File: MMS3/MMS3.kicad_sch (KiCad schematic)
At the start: 5 parts

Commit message: changed most of stuff to ch32L103
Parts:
- added Q1: MMBT5401 200-300, PCM_JLCPCB:Q_SOT-23, symbol PCM_JLCPCB-Transistors:PNP,MMBT5401 200-300
- added R10: 1.5kΩ, PCM_JLCPCB:R_0603, symbol PCM_JLCPCB-Resistors:0603,1.5kΩ
- added R12, R13: 5.1kΩ, PCM_JLCPCB:R_0603, symbol PCM_JLCPCB-Resistors:0603,5.1kΩ
- added TP5, TP6: TestPoint, TestPoint:TestPoint_Pad_D1.0mm, symbol Connector:TestPoint
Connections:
- net USB switch1/SEL is gone; now on net BRD_VIN: D5.2
- net GND: now also Q1.2 (E), R12.2, R13.2
- new net: Q1.1 (B), R10.2
- new net CAN.RX: TP6.1
- new net CAN.TX: TP5.1
- new net CC1: R13.1
- new net CC2: R12.1
- new net CH32L103/PC13 (TAMPER, RTC): R10.1
- new net RXD2_LED: Q1.3 (C)
- no-connect marks 2 -> 23
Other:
- removed sheet CAN_TR1
- removed sheet MCU
- removed sheet STlink-BMprobe
- removed sheet Slide-SW
- removed sheet USB HUB
- removed sheet USB switch
- removed sheet USB switch1
- removed sheet VRM
- added sheet CH32L103 (CH32L103C8T6.kicad_sch)
- sheet USBC_CONN ports: added CC1, CC2; removed none
- note added: "LDO 5V 3V3"
- note added: "USER BUTTON"
- note removed: "USB- Stealy Wheely"
- moved on the sheet: D5, H1, H2, H3, H4

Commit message: backup commit
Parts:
- removed R12, R13: 5.1kΩ, PCM_JLCPCB:R_0603, symbol PCM_JLCPCB-Resistors:0603,5.1kΩ
- removed TP5, TP6: TestPoint, TestPoint:TestPoint_Pad_D1.0mm, symbol Connector:TestPoint
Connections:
- net BRD_VIN: no longer D5.2
- net CH32L103/PC13 (TAMPER, RTC) renamed CH32L103_Wrapper/PC13
- new net USB_Data/VBUS: D5.2
- no-connect marks 23 -> 2
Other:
- sheet USBC_CONN renamed USB_Data
- removed sheet CH32L103
- added sheet CH32L103_Wrapper (CH32L103_MMS3.kicad_sch)
- added sheet Power Supply (LDO.kicad_sch)
- added sheet USB_PD (USP_PD.kicad_sch)
- sheet USB_Data ports: added none; removed CC1, CC2
- note added: "CAN"
- note added: "CHINESE"
- note added: "EEPROM"
- note added: "MCU"
- note added: "No MMS_Link USB Programmer due to budget cuts )):"
- note added: "PSU"

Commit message: kinda finished schematic
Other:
- removed sheet Power Supply
- added sheet VRM (VRM.kicad_sch)
- note removed: "CHINESE"
- note removed: "MCU"
- note removed: "PSU"

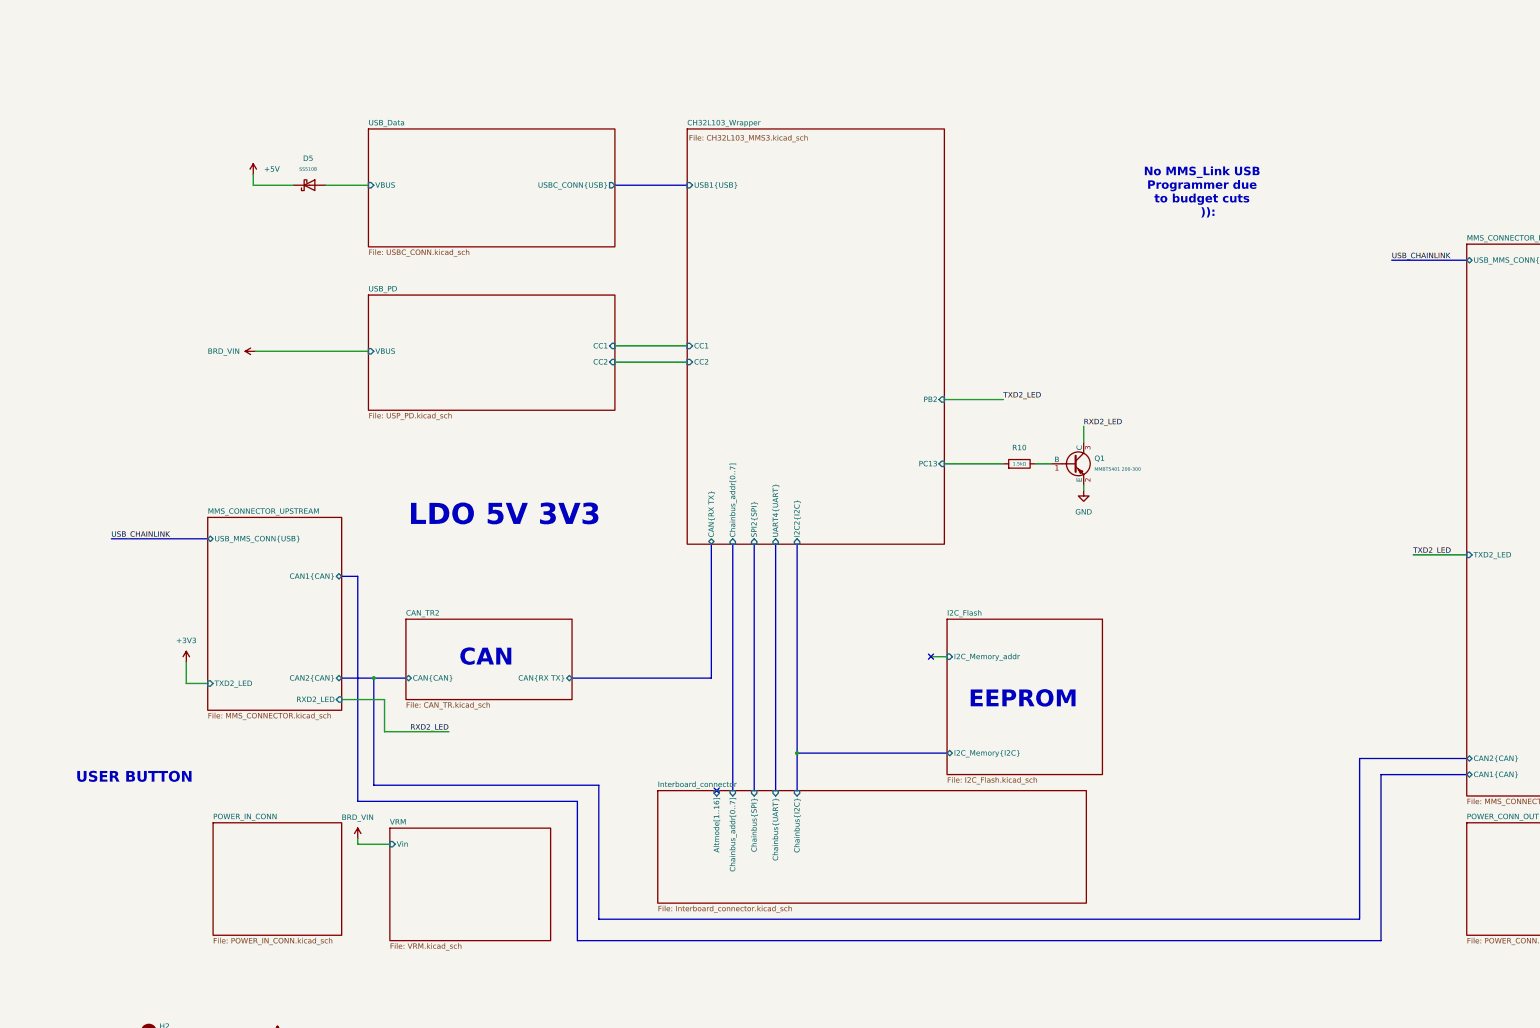
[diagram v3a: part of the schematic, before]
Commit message: updated schematic, removed annotation
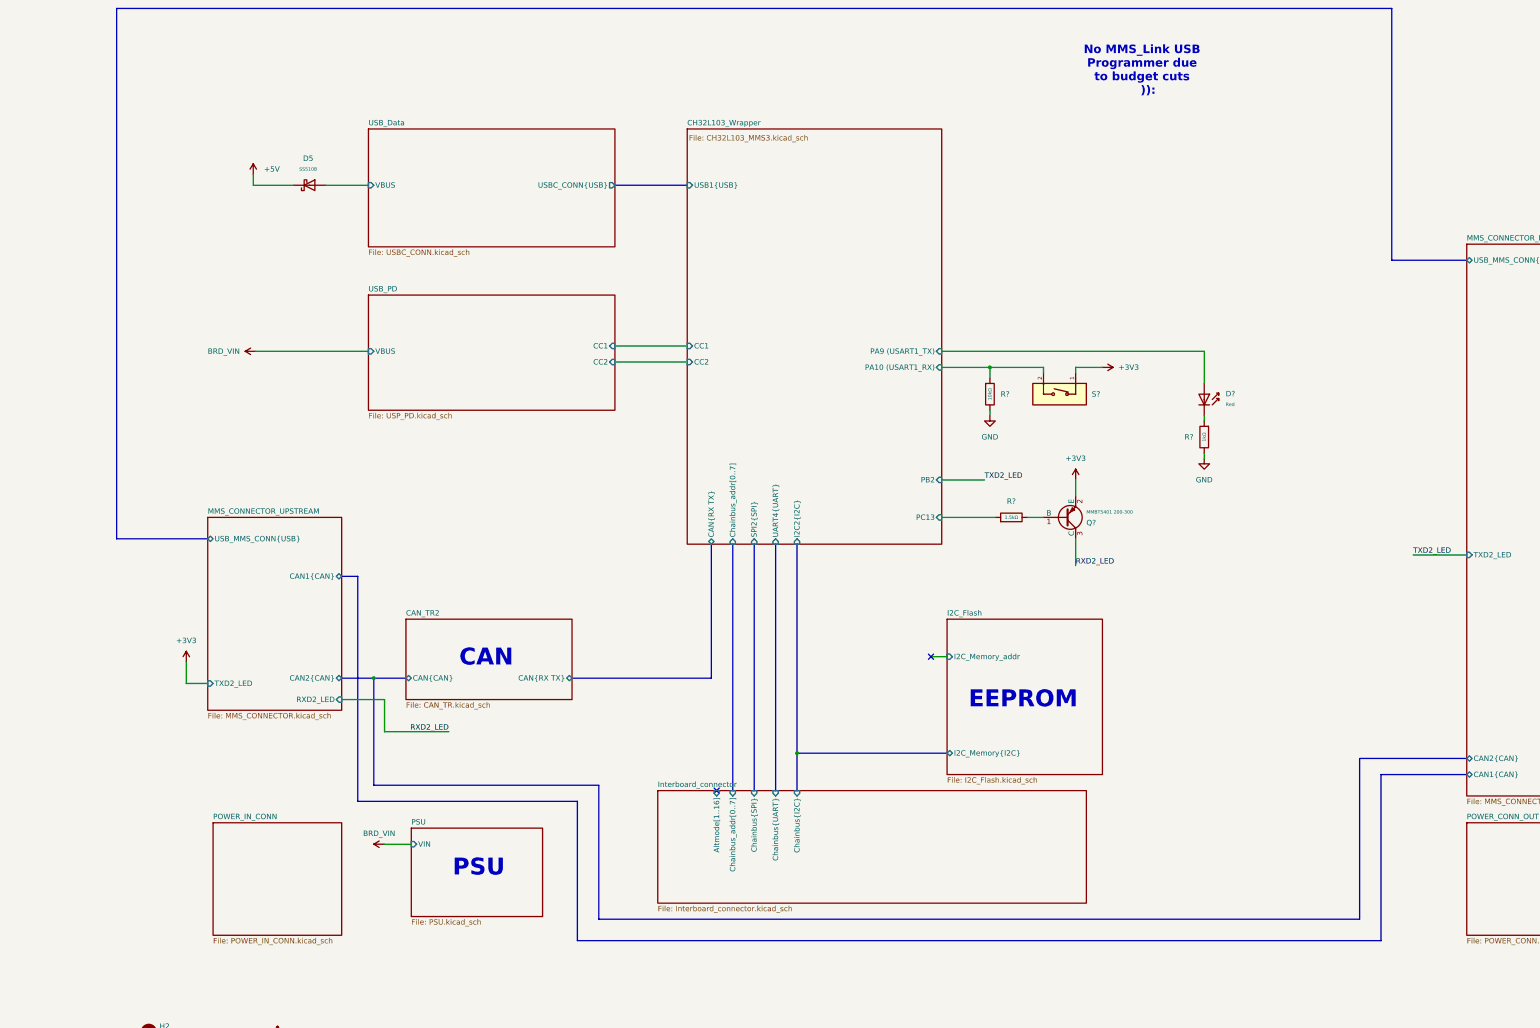
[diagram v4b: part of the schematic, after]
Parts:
- added D?: Red, PCM_JLCPCB:D_0603, symbol PCM_JLCPCB-Diodes:LED,0603,Red
- added R?: 10kΩ, PCM_JLCPCB:R_0402, symbol PCM_JLCPCB-Resistors:0402,10kΩ
- added R?: 1kΩ, PCM_JLCPCB:R_0603, symbol PCM_JLCPCB-Resistors:0603,1kΩ
- added S?: Tactile Button, 160gf, PCM_JLCPCB:SW_TS-1088-AR02016, symbol PCM_JLCPCB-Connectors_Buttons:Tactile Button, 160gf, 12V, 50mA, 4.0mm
- renumbered Q1 to Q?, R10 to R?
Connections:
- net +3V3: now also Q?.2 (E), S?.1 (A)
- net GND: now also R?.2, R?.2; no longer Q?.2 (E)
- new net: D?.1, R?.1
- new net CH32L103_Wrapper/PA10 (USART1_RX): R?.1, S?.2 (B)
- new net CH32L103_Wrapper/PA9 (USART1_TX): D?.2
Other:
- removed sheet VRM
- added sheet PSU (PSU.kicad_sch)
- sheet CH32L103_Wrapper ports: added PA10 (USART1_RX), PA9 (USART1_TX); removed none
- note added: "PSU"
- note removed: "LDO 5V 3V3"
- note removed: "USER BUTTON"
- title: MMS3 -> MMS3 CH32L103 Version
- moved on the sheet: Q?, R?

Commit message: initial PCB update
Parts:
- gave numbers to parts that had none: 6
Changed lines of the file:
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@@
 		(dnp no)
 		(fields_autoplaced yes)
-		(property "Reference" "R?"
+		(property "Reference" "R7"
 			(at 251.46 114.2999 0)
 			(show_name no)
@@
 			(project "MMS3"
 				(path "/712cea22-140d-4c92-923f-f4998caf3ecd"
-					(reference "R?")
+					(reference "R7")
 					(unit 1)
 				)
@@
 		(dnp no)
 		(fields_autoplaced yes)
-		(property "Reference" "#PWR?"
+		(property "Reference" "#PWR010"
 			(at 248.92 125.73 0)
 			(hide yes)
@@
 			(project "MMS3"
 				(path "/712cea22-140d-4c92-923f-f4998caf3ecd"
-					(reference "#PWR?")
+					(reference "#PWR010")
 					(unit 1)
 				)
@@
 		(in_pos_files yes)
 		(dnp no)
-		(property "Reference" "Q?"
+		(property "Reference" "Q1"
 			(at 271.78 144.7801 0)
 			(show_name no)
@@
 			(project "MMS3"
 				(path "/712cea22-140d-4c92-923f-f4998caf3ecd"
-					(reference "Q?")
+					(reference "Q1")
 					(unit 1)
 				)
@@
 		(dnp no)
 		(fields_autoplaced yes)
-		(property "Reference" "#PWR?"
+		(property "Reference" "#PWR012"
 			(at 271.78 107.95 0)
 			(hide yes)
@@
 			(project "MMS3"
 				(path "/712cea22-140d-4c92-923f-f4998caf3ecd"
-					(reference "#PWR?")
+					(reference "#PWR012")
 					(unit 1)
 				)
@@
 		(dnp no)
 		(fields_autoplaced yes)
-		(property "Reference" "S?"
+		(property "Reference" "S1"
 			(at 273.05 114.2999 90)
 			(show_name no)
@@
 			(project "MMS3"
 				(path "/712cea22-140d-4c92-923f-f4998caf3ecd"
-					(reference "S?")
+					(reference "S1")
 					(unit 1)
 				)
@@
 		(dnp no)
 		(fields_autoplaced yes)
-		(property "Reference" "R?"
+		(property "Reference" "R9"
 			(at 297.18 124.4599 0)
 			(show_name no)
@@
 			(project "MMS3"
 				(path "/712cea22-140d-4c92-923f-f4998caf3ecd"
-					(reference "R?")
+					(reference "R9")
 					(unit 1)
 				)
@@
 		(dnp no)
 		(fields_autoplaced yes)
-		(property "Reference" "R?"
+		(property "Reference" "R8"
 			(at 254 139.7 90)
 			(show_name no)
@@
 			(project "MMS3"
 				(path "/712cea22-140d-4c92-923f-f4998caf3ecd"
-					(reference "R?")
+					(reference "R8")
 					(unit 1)
 				)
@@
 		(dnp no)
 		(fields_autoplaced yes)
-		(property "Reference" "#PWR?"
+		(property "Reference" "#PWR011"
 			(at 269.24 138.43 0)
 			(hide yes)
@@
 			(project "MMS3"
 				(path "/712cea22-140d-4c92-923f-f4998caf3ecd"
-					(reference "#PWR?")
+					(reference "#PWR011")
 					(unit 1)
 				)
@@
 		(dnp no)
 		(fields_autoplaced yes)
-		(property "Reference" "#PWR?"
+		(property "Reference" "#PWR013"
 			(at 299.72 135.89 0)
 			(hide yes)
@@
 			(project "MMS3"
 				(path "/712cea22-140d-4c92-923f-f4998caf3ecd"
-					(reference "#PWR?")
+					(reference "#PWR013")
 					(unit 1)
 				)
@@
 		(dnp no)
 		(fields_autoplaced yes)
-		(property "Reference" "D?"
+		(property "Reference" "D1"
 			(at 304.8 114.2046 0)
 			(show_name no)
@@
 			(project "MMS3"
 				(path "/712cea22-140d-4c92-923f-f4998caf3ecd"
-					(reference "D?")
+					(reference "D1")
 					(unit 1)
 				)

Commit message: re-added onboard programmer
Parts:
- removed Q1: MMBT5401 200-300, PCM_JLCPCB:Q_SOT-23, symbol PCM_JLCPCB-Transistors:PNP,MMBT5401 200-300
- removed R8: 1.5kΩ, PCM_JLCPCB:R_0603, symbol PCM_JLCPCB-Resistors:0603,1.5kΩ
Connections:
- net CH32L103_Wrapper/PA10 (USART1_RX) renamed CH32L103_Wrapper/PB2
- net CH32L103_Wrapper/PA9 (USART1_TX) renamed CH32L103_Wrapper/PB3
- net USB_Data/VBUS renamed USB switch1/SEL
- no-connect marks 2 -> 1
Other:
- added sheet Slide-SW (Slide-SW.kicad_sch)
- added sheet USB HUB (USB HUB.kicad_sch)
- added sheet USB switch (USB switch.kicad_sch)
- added sheet USB switch1 (USB switch.kicad_sch)
- added sheet WCH-LinkE (WCH-LinkE.kicad_sch)
- sheet CH32L103_Wrapper ports: added Altmode[1..16], PB3, PB4, PB5, WCH-Link{WCH-Link}; removed PA10 (USART1_RX), PA9 (USART1_TX), PC13
- note added: "AltMode has only few pins on it"
- note added: "USB- Stealy Wheely"
- note added: "User Button"
- note added: "User LED"
- note removed: "No MMS_Link USB Programmer due to budget cuts )):"
- moved on the sheet: D1, D5, R7, R9, S1
